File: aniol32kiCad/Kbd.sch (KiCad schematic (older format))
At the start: 14 parts

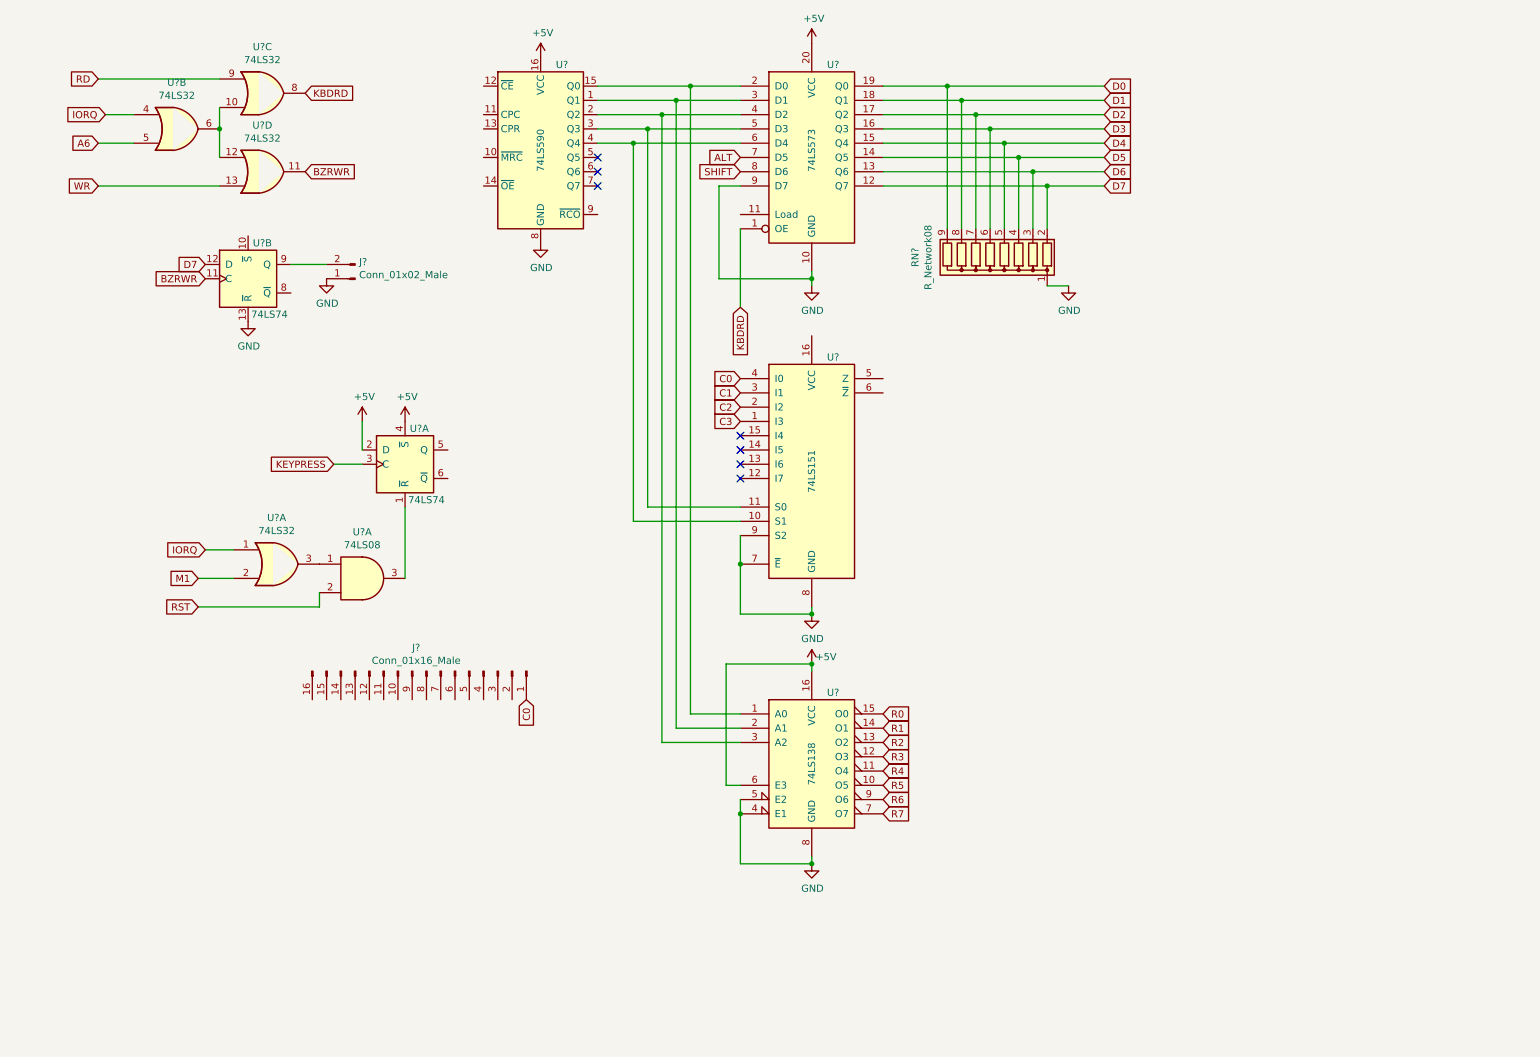
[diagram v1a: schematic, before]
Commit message: filling in the schematic
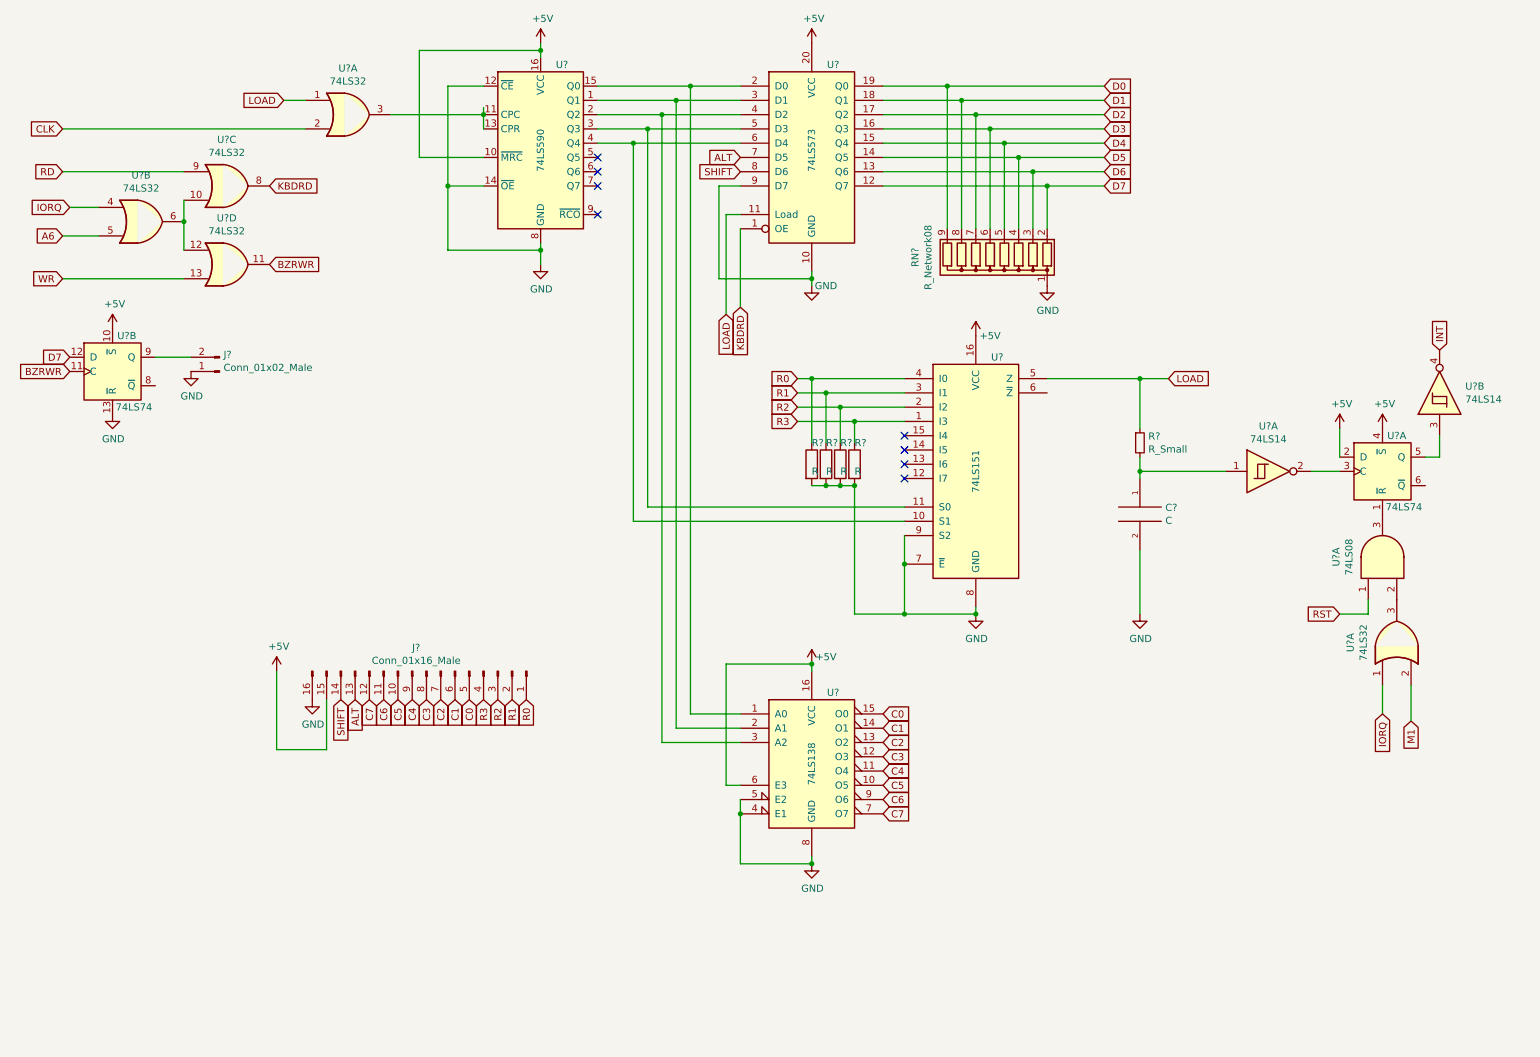
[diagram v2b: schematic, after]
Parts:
- added C?: C, symbol pspice:C
- added R? (x4): R, symbol Device:R
- added R?: R_Small, symbol Device:R_Small
- added U? (x2): 74LS14, symbol 74xx:74LS14
- added U?: 74LS32, symbol 74xx:74LS32
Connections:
- net R4 is gone; now on net C4: U?.11 (O4)
- net R5 is gone; now on net C5: U?.10 (O5)
- net R6 is gone; now on net C6: U?.9 (O6)
- net R7 is gone; now on net C7: U?.7 (O7)
- net +5V: now also J?.15 (Pin_15), U?.10 (~MRC), U?.10 (~S), U?.16 (VCC)
- net ALT: now also J?.13 (Pin_13)
- net C0: now also J?.5 (Pin_5), U?.15 (O0); no longer J?.1 (Pin_1), U?.4 (I0)
- net C1: now also J?.6 (Pin_6), U?.14 (O1); no longer U?.3 (I1)
- net C2: now also J?.7 (Pin_7), U?.13 (O2); no longer U?.2 (I2)
- net C3: now also J?.8 (Pin_8), U?.12 (O3); no longer U?.1 (I3)
- net GND: now also J?.16 (Pin_16), U?.12 (~CE), U?.14 (~OE), C?.2, R?.2, R?.2, R?.2, R?.2
- net R0: now also J?.1 (Pin_1), U?.4 (I0), R?.1; no longer U?.15 (O0)
- net R1: now also J?.2 (Pin_2), U?.3 (I1), R?.1; no longer U?.14 (O1)
- net R2: now also J?.3 (Pin_3), U?.2 (I2), R?.1; no longer U?.13 (O2)
- net R3: now also J?.4 (Pin_4), U?.1 (I3), R?.1; no longer U?.12 (O3)
- net RST: now also U?.1; no longer U?.2
- net SHIFT: now also J?.14 (Pin_14)
- net C5: now reaches J?.10 (Pin_10)
- net C6: now reaches J?.11 (Pin_11)
- net C7: now reaches J?.12 (Pin_12)
- net C4: now reaches J?.9 (Pin_9)
- net LOAD: now reaches U?.5 (Z)
- net LOAD: now also U?.11 (Load), R?.1, U?.1
- net at U?.11 (CPC): now also U?.13 (CPR), U?.3
- net at U?.5 (Q): now also U?.3
- net at U?.3: now also U?.2; no longer U?.1
- net KEYPRESS: no longer names the net of U?.3 (C)
- net KEYPRESS: now also U?.2
- new net: C?.1, R?.2, U?.1
- new net CLK: U?.2
- new net INT: U?.4
- no-connect marks 7 -> 8
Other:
- moved on the sheet: J?, U?, U?A, U?B, U?C, U?D

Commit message: some changes to schematic and var
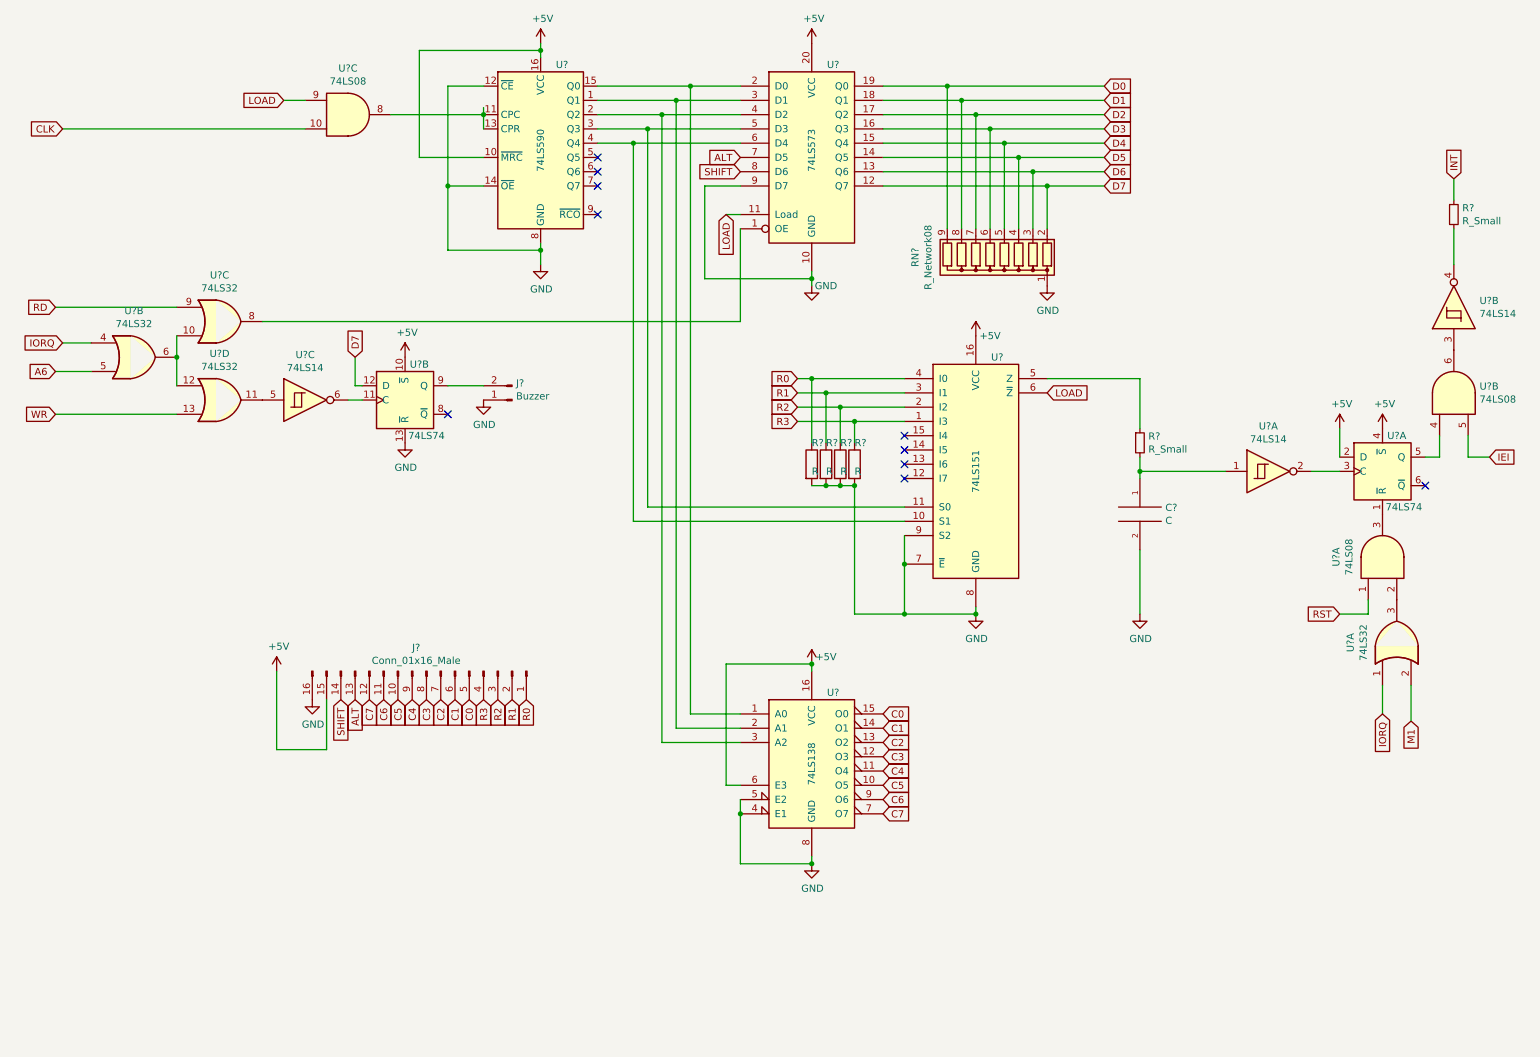
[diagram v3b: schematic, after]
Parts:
- removed U?: 74LS32, symbol 74xx:74LS32
- added R?: R_Small, symbol Device:R_Small
- added U? (x2): 74LS08, symbol 74xx:74LS08
- added U?: 74LS14, symbol 74xx:74LS14
- J?: value Conn_01x02_Male -> Buzzer
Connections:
- net CLK: now also U?.10
- net INT: now also R?.1; no longer U?.4
- net LOAD: now also U?.6 (~Z), U?.9; no longer R?.1, U?.5 (Z)
- net at U?.11 (CPC), U?.13 (CPR): now also U?.8
- net at U?.5 (Q): now also U?.4; no longer U?.3
- net BZRWR: no longer names the net of U?.11
- net BZRWR: now also U?.5; no longer U?.11 (C)
- net KBDRD: no longer names the net of U?.1 (OE), U?.8
- new net: U?.3, U?.6
- new net: R?.2, U?.4
- new net: R?.1, U?.5 (Z)
- new net: U?.11 (C), U?.6
- new net IEI: U?.5
- no-connect marks 8 -> 10
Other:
- moved on the sheet: J?, U?B, U?C, U?D
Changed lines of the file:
@@
 L 74xx:74LS32 U?
 U 2 1 61AFC13A
-P 1450 2000
+P 1400 2950
 AR Path="/61AFC13A" Ref="U?"  Part="2"
 AR Path="/61AEA36E/61AFC13A" Ref="U?"  Part="2"
-F 0 "U?" H 1450 2325 50  0000 C CNN
-F 1 "74LS32" H 1450 2234 50  0000 C CNN
-F 2 "" H 1450 2000 50  0001 C CNN
-F 3 "http://www.ti.com/lit/gpn/sn74LS32" H 1450 2000 50  0001 C CNN
-	2    1450 2000
+F 0 "U?" H 1400 3275 50  0000 C CNN
+F 1 "74LS32" H 1400 3184 50  0000 C CNN
+F 2 "" H 1400 2950 50  0001 C CNN
+F 3 "http://www.ti.com/lit/gpn/sn74LS32" H 1400 2950 50  0001 C CNN
+	2    1400 2950
 	1    0    0    -1
 $EndComp
@@
 L 74xx:74LS32 U?
 U 4 1 61AFC140
-P 2050 2300
+P 2000 3250
 AR Path="/61AFC140" Ref="U?"  Part="4"
 AR Path="/61AEA36E/61AFC140" Ref="U?"  Part="4"
-F 0 "U?" H 2050 2625 50  0000 C CNN
-F 1 "74LS32" H 2050 2534 50  0000 C CNN
-F 2 "" H 2050 2300 50  0001 C CNN
-F 3 "http://www.ti.com/lit/gpn/sn74LS32" H 2050 2300 50  0001 C CNN
-	4    2050 2300
-	1    0    0    -1
-$EndComp
-Wire Wire Line
-	1750 2200 1750 2000
-Wire Wire Line
-	1750 2000 1750 1850
-Connection ~ 1750 2000
-Text GLabel 950  1900 0    50   Input ~ 0
+F 0 "U?" H 2000 3575 50  0000 C CNN
+F 1 "74LS32" H 2000 3484 50  0000 C CNN
+F 2 "" H 2000 3250 50  0001 C CNN
+F 3 "http://www.ti.com/lit/gpn/sn74LS32" H 2000 3250 50  0001 C CNN
+	4    2000 3250
+	1    0    0    -1
+$EndComp
+Wire Wire Line
+	1700 3150 1700 2950
+Wire Wire Line
+	1700 2950 1700 2800
+Connection ~ 1700 2950
+Text GLabel 900  2850 0    50   Input ~ 0
 IORQ
 Wire Wire Line
-	1150 1900 950  1900
-Text GLabel 900  2100 0    50   Input ~ 0
+	1100 2850 900  2850
+Text GLabel 850  3050 0    50   Input ~ 0
 A6
 Wire Wire Line
-	1150 2100 900  2100
-Text GLabel 900  1650 0    50   Input ~ 0
+	1100 3050 850  3050
+Text GLabel 850  2600 0    50   Input ~ 0
 RD
 Wire Wire Line
-	900  1650 1750 1650
-Text GLabel 900  2400 0    50   Input ~ 0
+	850  2600 1700 2600
+Text GLabel 850  3350 0    50   Input ~ 0
 WR
 Wire Wire Line
-	900  2400 1750 2400
-Text GLabel 2350 1750 2    50   Input ~ 0
-KBDRD
+	850  3350 1700 3350
 $Comp
 L 74xx:74LS32 U?
 U 3 1 61AFC152
-P 2050 1750
+P 2000 2700
 AR Path="/61AFC152" Ref="U?"  Part="3"
 AR Path="/61AEA36E/61AFC152" Ref="U?"  Part="3"
-F 0 "U?" H 2050 2075 50  0000 C CNN
-F 1 "74LS32" H 2050 1984 50  0000 C CNN
-F 2 "" H 2050 1750 50  0001 C CNN
-F 3 "http://www.ti.com/lit/gpn/sn74LS32" H 2050 1750 50  0001 C CNN
-	3    2050 1750
-	1    0    0    -1
-$EndComp
-Text GLabel 2350 2300 2    50   Input ~ 0
-BZRWR
+F 0 "U?" H 2000 3025 50  0000 C CNN
+F 1 "74LS32" H 2000 2934 50  0000 C CNN
+F 2 "" H 2000 2700 50  0001 C CNN
+F 3 "http://www.ti.com/lit/gpn/sn74LS32" H 2000 2700 50  0001 C CNN
+	3    2000 2700
+	1    0    0    -1
+$EndComp
 Text GLabel 4150 5350 3    50   Input ~ 0
 R0
@@
 	1    0    0    -1
 $EndComp
-Wire Wire Line
-	5650 2600 5650 2050
-Text GLabel 5650 2600 3    50   Input ~ 0
-KBDRD
 $Comp
 L power:GND #PWR?
@@
 Wire Wire Line
 	6150 2400 6150 2450
-Wire Wire Line
-	5500 1750 5500 2400
-Wire Wire Line
-	6150 2400 5500 2400
 Connection ~ 6150 2400
 Wire Wire Line
 	6150 2350 6150 2400
-Wire Wire Line
-	5650 1750 5500 1750
 NoConn ~ 4650 1750
 NoConn ~ 4650 1650
@@
 L 74xx:74LS74 U?
 U 2 1 61B1EDAC
-P 1250 3050
+P 3300 3250
 AR Path="/61B1EDAC" Ref="U?"  Part="2"
 AR Path="/61AEA36E/61B1EDAC" Ref="U?"  Part="2"
-F 0 "U?" H 1350 3300 50  0000 C CNN
-F 1 "74LS74" H 1400 2800 50  0000 C CNN
-F 2 "" H 1250 3050 50  0001 C CNN
-F 3 "74xx/74hc_hct74.pdf" H 1250 3050 50  0001 C CNN
-	2    1250 3050
+F 0 "U?" H 3400 3500 50  0000 C CNN
+F 1 "74LS74" H 3450 3000 50  0000 C CNN
+F 2 "" H 3300 3250 50  0001 C CNN
+F 3 "74xx/74hc_hct74.pdf" H 3300 3250 50  0001 C CNN
+	2    3300 3250
 	1    0    0    -1
 $EndComp
@@
 Wire Wire Line
 	7800 1750 6650 1750
-Text GLabel 950  2950 0    50   Input ~ 0
+Text GLabel 2950 2950 1    50   Input ~ 0
 D7
-Text GLabel 950  3050 0    50   Input ~ 0
-BZRWR
 $Comp
 L Connector:Conn_01x02_Male J?
 U 1 1 61B45D9D
-P 2000 3050
-F 0 "J?" H 1972 2932 50  0000 R CNN
-F 1 "Conn_01x02_Male" H 1972 3023 50  0000 R CNN
-F 2 "" H 2000 3050 50  0001 C CNN
-F 3 "~" H 2000 3050 50  0001 C CNN
-	1    2000 3050
+P 4050 3250
+F 0 "J?" H 4022 3132 50  0000 R CNN
+F 1 "Buzzer" H 4022 3223 50  0000 R CNN
+F 2 "" H 4050 3250 50  0001 C CNN
+F 3 "~" H 4050 3250 50  0001 C CNN
+	1    4050 3250
 	-1   0    0    1
 $EndComp
 Wire Wire Line
-	1800 2950 1550 2950
+	3850 3150 3600 3150
 $Comp
 L power:GND #PWR?
 U 1 1 61B4867B
-P 1800 3050
-F 0 "#PWR?" H 1800 2800 50  0001 C CNN
-F 1 "GND" H 1805 2877 50  0000 C CNN
-F 2 "" H 1800 3050 50  0001 C CNN
-F 3 "" H 1800 3050 50  0001 C CNN
-	1    1800 3050
+P 3850 3250
+F 0 "#PWR?" H 3850 3000 50  0001 C CNN
+F 1 "GND" H 3855 3077 50  0000 C CNN
+F 2 "" H 3850 3250 50  0001 C CNN
+F 3 "" H 3850 3250 50  0001 C CNN
+	1    3850 3250
 	1    0    0    -1
 $EndComp
@@
 L power:GND #PWR?
 U 1 1 61B48E69
-P 1250 3350
-F 0 "#PWR?" H 1250 3100 50  0001 C CNN
-F 1 "GND" H 1255 3177 50  0000 C CNN
-F 2 "" H 1250 3350 50  0001 C CNN
-F 3 "" H 1250 3350 50  0001 C CNN
-	1    1250 3350
+P 3300 3550
+F 0 "#PWR?" H 3300 3300 50  0001 C CNN
+F 1 "GND" H 3305 3377 50  0000 C CNN
+F 2 "" H 3300 3550 50  0001 C CNN
+F 3 "" H 3300 3550 50  0001 C CNN
+	1    3300 3550
 	1    0    0    -1
 $EndComp
@@
 L power:+5V #PWR?
 U 1 1 618DBCE9
-P 1250 2750
-F 0 "#PWR?" H 1250 2600 50  0001 C CNN
-F 1 "+5V" H 1265 2923 50  0000 C CNN
-F 2 "" H 1250 2750 50  0001 C CNN
-F 3 "" H 1250 2750 50  0001 C CNN
-	1    1250 2750
+P 3300 2950
+F 0 "#PWR?" H 3300 2800 50  0001 C CNN
+F 1 "+5V" H 3315 3123 50  0000 C CNN
+F 2 "" H 3300 2950 50  0001 C CNN
+F 3 "" H 3300 2950 50  0001 C CNN
+	1    3300 2950
 	1    0    0    -1
 $EndComp
@@
 	6350 3850 6450 3850
 Connection ~ 6800 4750
-Text GLabel 8650 3100 2    50   Input ~ 0
+Text GLabel 7800 3200 2    50   Input ~ 0
 LOAD
-Wire Wire Line
-	8650 3100 8450 3100
-Connection ~ 8450 3100
-Text GLabel 5550 2650 3    50   Input ~ 0
+Text GLabel 5550 1950 3    50   Input ~ 0
 LOAD
 Wire Wire Line
-	5550 2650 5550 1950
-Wire Wire Line
 	5550 1950 5650 1950
-$Comp
-L 74xx:74LS32 U?
-U 1 1 618ED8CC
-P 2900 1250
-F 0 "U?" H 2900 1575 50  0000 C CNN
-F 1 "74LS32" H 2900 1484 50  0000 C CNN
-F 2 "" H 2900 1250 50  0001 C CNN
-F 3 "http://www.ti.com/lit/gpn/sn74LS32" H 2900 1250 50  0001 C CNN
-	1    2900 1250
-	1    0    0    -1
-$EndComp
 Text GLabel 900  1350 0    50   Input ~ 0
 CLK
@@
 L 74xx:74LS14 U?
 U 2 1 61948336
-P 10550 3200
-F 0 "U?" V 10596 3020 50  0000 R CNN
-F 1 "74LS14" V 10505 3020 50  0000 R CNN
-F 2 "" H 10550 3200 50  0001 C CNN
-F 3 "http://www.ti.com/lit/gpn/sn74LS14" H 10550 3200 50  0001 C CNN
-	2    10550 3200
+P 10650 2600
+F 0 "U?" V 10696 2420 50  0000 R CNN
+F 1 "74LS14" V 10605 2420 50  0000 R CNN
+F 2 "" H 10650 2600 50  0001 C CNN
+F 3 "http://www.ti.com/lit/gpn/sn74LS14" H 10650 2600 50  0001 C CNN
+	2    10650 2600
 	0    -1   -1   0
 $EndComp
@@
 Wire Wire Line
 	10550 3650 10550 3500
-Text GLabel 10550 2900 1    50   Input ~ 0
+Text GLabel 10650 1700 1    50   Input ~ 0
 INT
+$Comp
+L 74xx:74LS08 U?
+U 2 1 618C3040
+P 10650 3200
+F 0 "U?" V 10696 3020 50  0000 R CNN
+F 1 "74LS08" V 10605 3020 50  0000 R CNN
+F 2 "" H 10650 3200 50  0001 C CNN
+F 3 "http://www.ti.com/lit/gpn/sn74LS08" H 10650 3200 50  0001 C CNN
+	2    10650 3200
+	0    -1   -1   0
+$EndComp
+Text GLabel 10900 3650 2    50   Input ~ 0
+IEI
+Wire Wire Line
+	10900 3650 10750 3650
+Wire Wire Line
+	10750 3650 10750 3500
+$Comp
+L 74xx:74LS08 U?
+U 3 1 618CEFDA
+P 2900 1250
+F 0 "U?" H 2900 1575 50  0000 C CNN
+F 1 "74LS08" H 2900 1484 50  0000 C CNN
+F 2 "" H 2900 1250 50  0001 C CNN
+F 3 "http://www.ti.com/lit/gpn/sn74LS08" H 2900 1250 50  0001 C CNN
+	3    2900 1250
+	1    0    0    -1
+$EndComp
+$Comp
+L 74xx:74LS14 U?
+U 3 1 618F15ED
+P 2600 3250
+F 0 "U?" H 2600 3567 50  0000 C CNN
+F 1 "74LS14" H 2600 3476 50  0000 C CNN
+F 2 "" H 2600 3250 50  0001 C CNN
+F 3 "http://www.ti.com/lit/gpn/sn74LS14" H 2600 3250 50  0001 C CNN
+	3    2600 3250
+	1    0    0    -1
+$EndComp
+Wire Wire Line
+	3000 3250 2900 3250
+Wire Wire Line
+	2950 3150 3000 3150
+$Comp
+L Device:R_Small R?
+U 1 1 618C449E
+P 10650 1950
+F 0 "R?" H 10709 1996 50  0000 L CNN
+F 1 "R_Small" H 10709 1905 50  0000 L CNN
+F 2 "" H 10650 1950 50  0001 C CNN
+F 3 "~" H 10650 1950 50  0001 C CNN
+	1    10650 1950
+	1    0    0    -1
+$EndComp
+Wire Wire Line
+	10650 1850 10650 1700
+Wire Wire Line
+	10650 2050 10650 2300
+Wire Wire Line
+	2950 2950 2950 3150
+Wire Wire Line
+	2300 2700 5650 2700
+Wire Wire Line
+	5650 2050 5650 2700
+Wire Wire Line
+	5400 2400 5400 1750
+Wire Wire Line
+	5400 2400 6150 2400
+Wire Wire Line
+	5400 1750 5650 1750
+NoConn ~ 10450 3850
+NoConn ~ 3600 3350
 $EndSCHEMATC
